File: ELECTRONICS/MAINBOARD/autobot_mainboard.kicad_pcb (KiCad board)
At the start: 4 copper layers, 50 x 38.5 mm, 170 parts, among them IC1 DW3210, J1 USB_C_Receptacle_USB2.0_16P, J10 Conn_01x05_Socket, J11 Conn_01x01_Socket, J12 Conn_01x02_Pin, J13 Conn_01x01_Socket, J17 Conn_01x02_Pin, J18 Conn_01x02_Pin, J19 Conn_02x05_Odd_Even, J2 Conn_01x01_Socket, J20 Conn_02x05_Odd_Even, J3 Conn_01x01_Socket, J4 Conn_01x02_Socket, J5 Conn_01x01_Socket, J6 Conn_01x01_Socket, J7 Conn_01x03_Pin, J8 Conn_Coaxial, J9 Conn_Coaxial, Q1 DMG1012T, Q2 DMG1012T, Q3 DMG1012T, Q4 DMG1012T, Q5 DMG1012T, SW1 RESET, SW2 BOOT, SW3 SW_Push, U1 TVS1400DRV, U10 VL53L1X, U11 VL53L1X, U12 VL53L1X, U13 BMI270, U14 BMI270, U16 LP5907MFX-3.3, U18 LP5907MFX-3.3, U19 STM32H743VITx, U2 LMR51430XDDCR, U23 LP5907MFX-3.3, U3 LP5907MFX-3.3, U4 TPD2EUSB30A, U7 STM32G031C_4-6-8_Tx, U9 VL53L1X, Y1 TXC 8Y38472012, Y2 25mhz placeholder

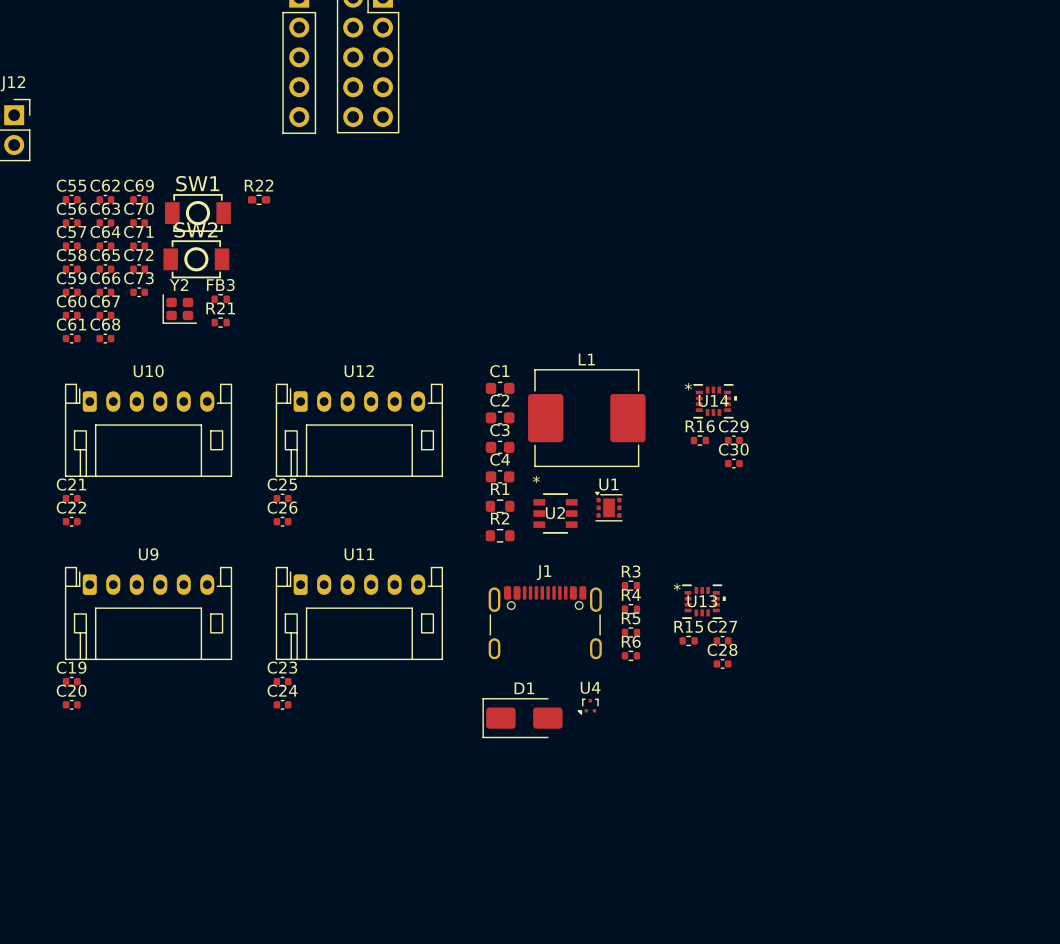
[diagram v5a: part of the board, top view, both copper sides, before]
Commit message: buck converter prelim route
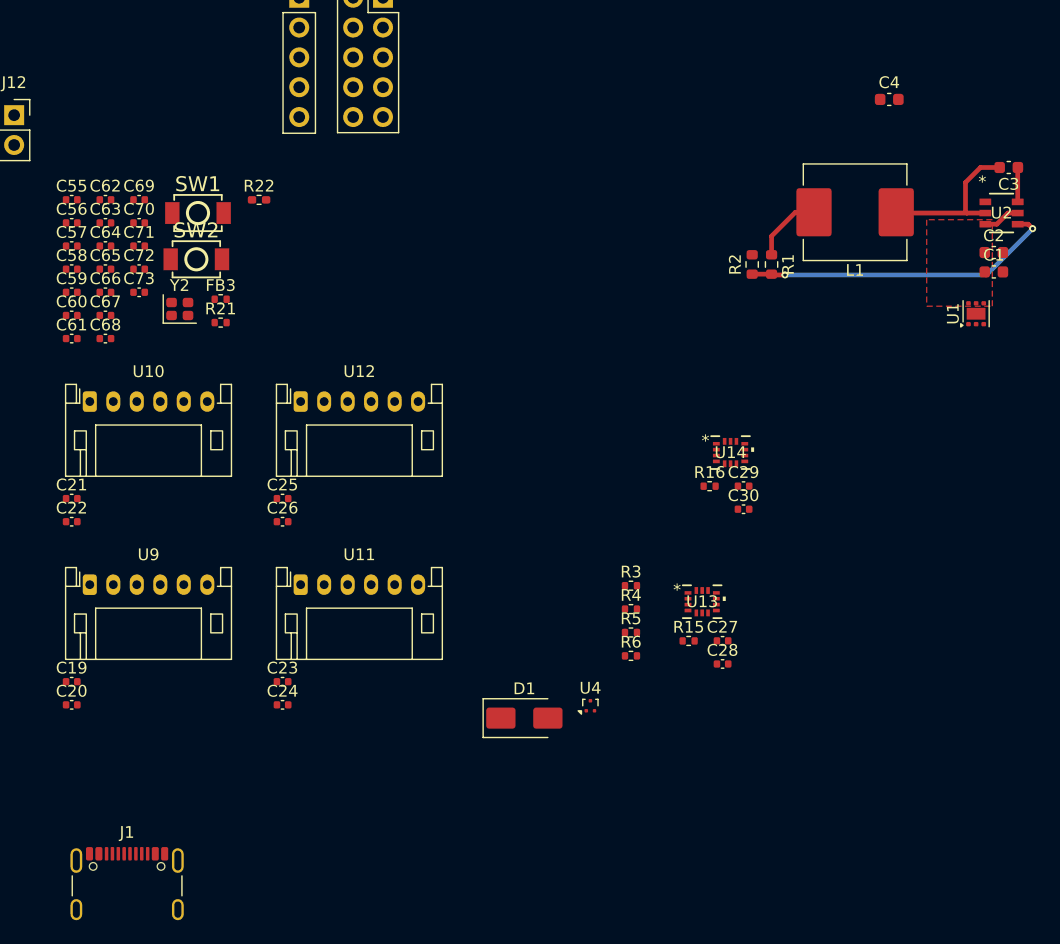
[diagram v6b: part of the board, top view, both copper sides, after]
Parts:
- moved C3 49.4 mm to (360.2, 58.2), turned to 180 degrees
- moved C4 46.1 mm to (350.0, 52.4)
- moved U2 45.8 mm to (359.6, 62.0)
- moved C2 44.3 mm to (358.9, 65.4)
- moved C1 43.2 mm to (358.9, 67.1)
- moved J1 42.0 mm to (285.1, 120.3)
- moved U1 35.4 mm to (357.4, 70.6), turned to 90 degrees
- moved R2 31.5 mm to (338.3, 66.4), turned to 90 degrees
- moved R1 31.0 mm to (340.0, 66.4), turned to -90 degrees
- moved L1 28.8 mm to (347.1, 62.0), turned to 180 degrees
- moved U14 4.60 mm to (336.5, 82.4)
- moved R16 3.97 mm to (334.7, 85.3)
- moved C29 3.97 mm to (337.6, 85.3)
- moved C30 3.97 mm to (337.6, 87.3)
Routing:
- net Net-(U2-FB): track 0.00 -> 27.0 mm, vias 0 -> 2
- net Net-(U2-SW): track 0.00 -> 13.7 mm
- net +5V: track 63.9 -> 69.9 mm
- net /LMR51430XDDCR/12V: track 0.00 -> 3.15 mm
- net Net-(U2-CB): track 0.00 -> 2.93 mm
- added copper zone on F.Cu, net /LMR51430XDDCR/12V
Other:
- board text added: "DOUBLE CHECK TVS DIODE DIRECTION"

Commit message: bmi routing
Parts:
- removed R15, R16: 10k, Resistor_SMD:R_0402_1005Metric
- moved C4 135.4 mm to (222.1, 96.7)
- moved C3 109.0 mm to (266.5, 114.0)
- moved C2 109.0 mm to (265.3, 121.3)
- moved C1 109.0 mm to (265.3, 122.8)
- moved U2 108.9 mm to (266.1, 117.8)
- moved L1 108.9 mm to (253.6, 117.7)
- moved U1 108.9 mm to (263.9, 126.4)
- moved R1 86.6 mm to (270.3, 117.9), turned to 180 degrees
- moved R2 86.3 mm to (270.3, 119.6), turned to 0 degrees
- moved R4 8.45 mm to (320.3, 92.3)
- moved R3 8.45 mm to (320.3, 90.3)
- moved R5 8.45 mm to (320.3, 94.3)
- moved R6 8.45 mm to (320.3, 96.3)
- moved C29 4.11 mm to (335.0, 82.1), turned to -90 degrees
- moved C30 2.52 mm to (336.7, 84.9), turned to 180 degrees
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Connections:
- U13 pad 9: unconnected-(U13-INT2-Pad9) -> /BMI270_L/BMI_INT
- U14 pad 9: unconnected-(U14-INT2-Pad9) -> /BMI270_R/BMI_INT
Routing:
- net +5V: track 69.9 -> 96.9 mm
- net Net-(U2-FB): track 27.0 -> 6.41 mm, vias 2 -> 1
- net /BMI270_R/BMI_INT: track 0.00 -> 9.36 mm, vias 0 -> 1
- net GNDREF: track 55.2 -> 61.1 mm
- net /DW3220_T/WAKEUP: track 0.73 -> 6.19 mm
- net /DW3220_T/RESET: track 0.73 -> 5.57 mm
- net /DW3220_T/SPICLK: track 0.73 -> 5.37 mm
- net /LMR51430XDDCR/12V: track 3.15 -> 6.90 mm, vias 0 -> 2
- net /BMI270_R/BMI_MISO: track 0.00 -> 3.31 mm
- net /BMI270_R/BMI_MOSI: track 0.00 -> 2.00 mm
- net /BMI270_R/BMI_SCK: track 0.00 -> 1.90 mm
- net /BMI270_R/BMI_CS: track 0.00 -> 1.80 mm
- net /DW3220_T/MISO: track 0.00 -> 0.62 mm
- net Net-(U2-SW): track 13.7 -> 13.1 mm, vias 0 -> 2
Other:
- board size 50 x 38.5 mm -> 268 x 112 mm

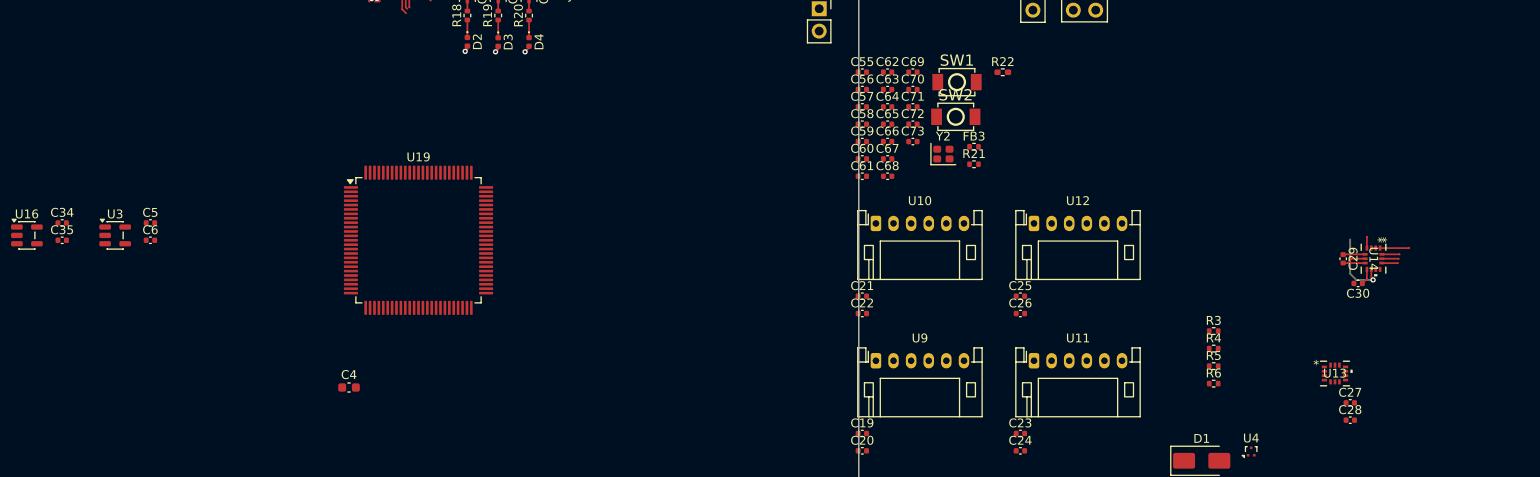
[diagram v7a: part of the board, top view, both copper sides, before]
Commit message: decoup cap on h743
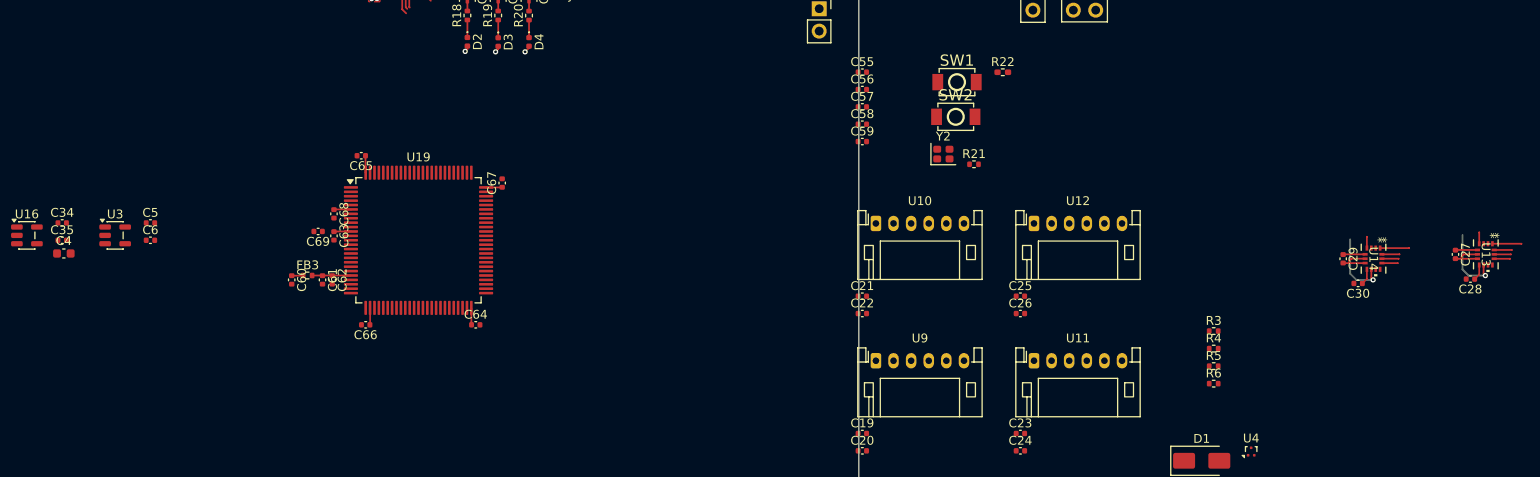
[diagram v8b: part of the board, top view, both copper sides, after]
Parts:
- removed the C69 at (286.1, 60.9)
- removed C70, C71, C72: 100n, Capacitor_SMD:C_0402_1005Metric
- moved FB3 77.1 mm to (217.4, 84.0)
- moved C69 68.3 mm to (218.6, 79.0), turned to 180 degrees
- moved C62 67.3 mm to (220.2, 84.5), turned to -90 degrees
- moved C60 66.2 mm to (215.6, 84.5), turned to -90 degrees
- moved C63 65.0 mm to (220.4, 79.5), turned to -90 degrees
- moved C68 63.0 mm to (220.4, 77.0), turned to -90 degrees
- moved C66 62.8 mm to (224.0, 89.6), turned to 180 degrees
- moved C61 62.4 mm to (219.1, 84.5), turned to -90 degrees
- moved C65 59.9 mm to (223.5, 70.4), turned to 180 degrees
- moved C64 52.9 mm to (236.5, 89.6)
- moved C67 43.9 mm to (239.5, 73.5), turned to 90 degrees
- moved C4 35.8 mm to (189.7, 81.5)
- moved U13 21.8 mm to (351.2, 81.6), turned to -90 degrees
- moved C28 21.0 mm to (349.5, 84.4), turned to 180 degrees
- moved C27 20.7 mm to (347.8, 81.6), turned to -90 degrees
- renumbered C73 to C69
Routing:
- net +3V3: track 82.6 -> 95.7 mm
- net /BMI270_L/BMI_INT: track 0.00 -> 9.36 mm, vias 0 -> 1
- net GNDREF: track 61.1 -> 65.8 mm
- net Net-(U19-VDDA): track 0.00 -> 4.41 mm
- net +5V: track 96.9 -> 101.2 mm
- net /BMI270_L/BMI_MISO: track 0.00 -> 3.31 mm
- net /BMI270_L/BMI_MOSI: track 0.00 -> 2.00 mm
- net /BMI270_L/BMI_SCK: track 0.00 -> 1.90 mm
- net /BMI270_L/BMI_CS: track 0.00 -> 1.80 mm
